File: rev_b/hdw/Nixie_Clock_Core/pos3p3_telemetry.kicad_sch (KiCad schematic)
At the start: 7 parts, among them U501 INA219BxDCN, U502 MCP9804

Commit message: lots of rev B control board schematic progress
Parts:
- renumbered C503 to C?, C502 to C?, C501 to C?, DOC501 to DOC?, DOC502 to DOC?, U502 to U?, U501 to U?

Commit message: more rev b sch progress
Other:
- moved on the sheet: C?

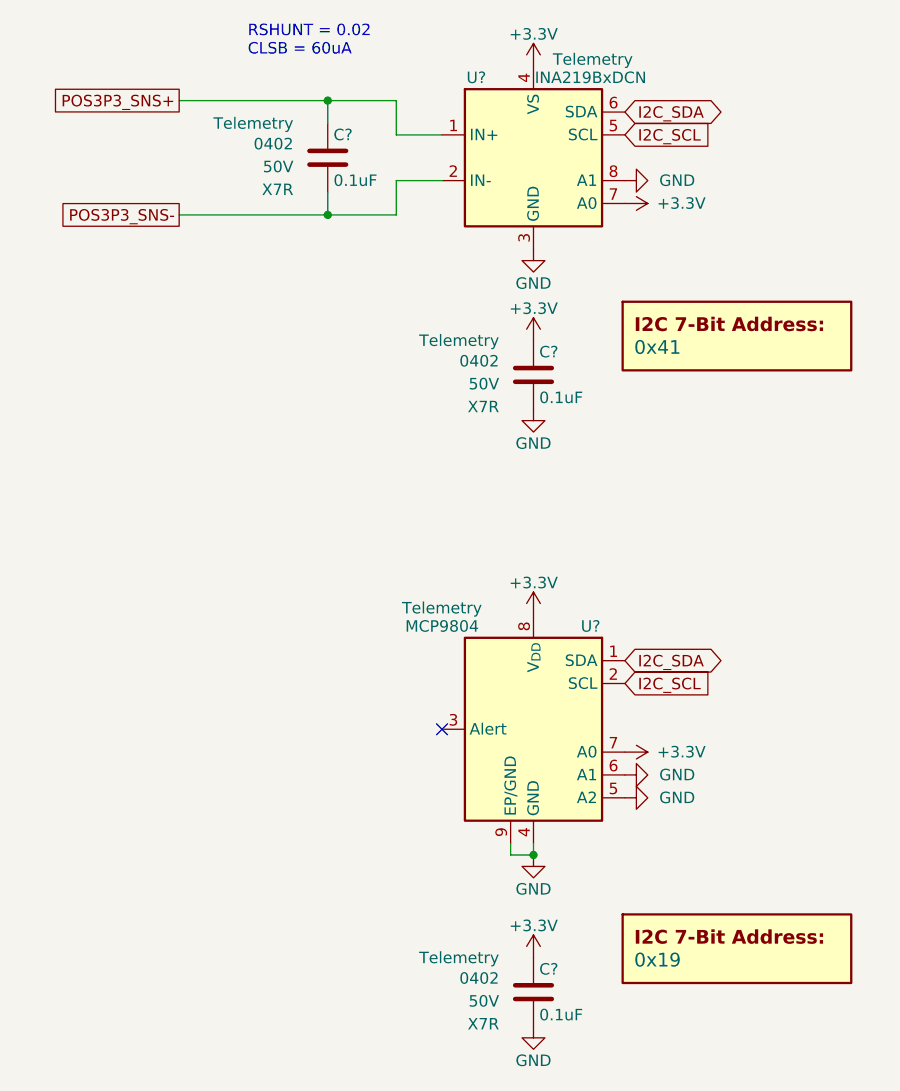
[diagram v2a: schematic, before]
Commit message: updated footprints, ran some DRC
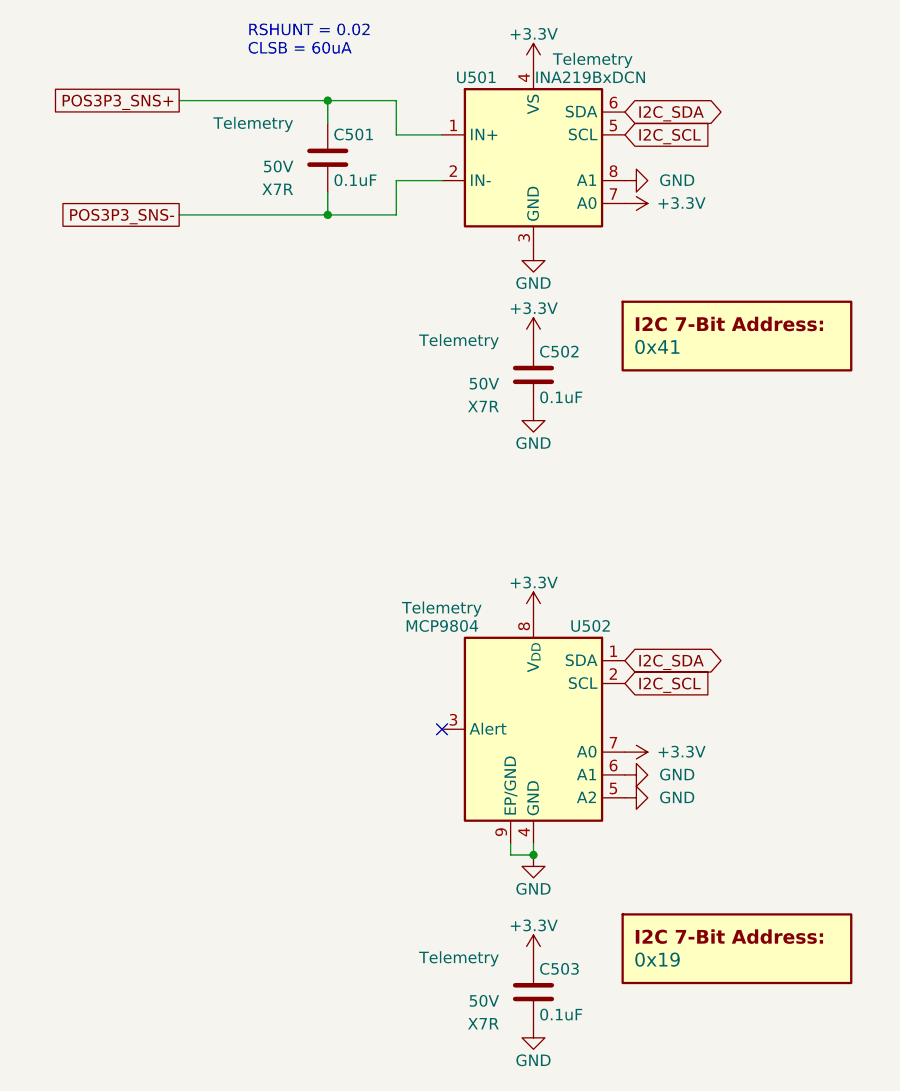
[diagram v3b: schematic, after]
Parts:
- C501, C502, C503: renamed from C?; footprint Capacitors_SMD:C_0402 -> Capacitors_SMD:C_0603; Digi-Key PN 490-10698-1-ND -> (none); display_footprint 0402 -> (none)
- gave numbers to parts that had none: 4

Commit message: hid all passive refdes on core PCB
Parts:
- C501, C502, C503: Digi-Key PN (none) -> 1276-1935-1-ND; display_footprint (none) -> 0603
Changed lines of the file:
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@@
       (effects (font (size 1.27 1.27)) hide)
     )
-    (property "display_footprint" "" (at 125.73 149.606 0)
+    (property "display_footprint" "0603" (at 125.73 149.606 0)
       (effects (font (size 1.27 1.27)) (justify right))
     )
@@
       (effects (font (size 1.27 1.27)) (justify right))
     )
-    (property "Digi-Key PN" "" (at 129.54 151.13 0)
+    (property "Digi-Key PN" "1276-1935-1-ND" (at 129.54 151.13 0)
       (effects (font (size 1.27 1.27)) hide)
     )
@@
       (effects (font (size 1.27 1.27)) hide)
     )
-    (property "display_footprint" "" (at 125.73 81.026 0)
+    (property "display_footprint" "0603" (at 125.73 81.026 0)
       (effects (font (size 1.27 1.27)) (justify right))
     )
@@
       (effects (font (size 1.27 1.27)) (justify right))
     )
-    (property "Digi-Key PN" "" (at 129.54 82.55 0)
+    (property "Digi-Key PN" "1276-1935-1-ND" (at 129.54 82.55 0)
       (effects (font (size 1.27 1.27)) hide)
     )
@@
       (effects (font (size 1.27 1.27)) hide)
     )
-    (property "display_footprint" "" (at 102.87 56.896 0)
+    (property "display_footprint" "0603" (at 102.87 56.896 0)
       (effects (font (size 1.27 1.27)) (justify right))
     )
@@
       (effects (font (size 1.27 1.27)) (justify right))
     )
-    (property "Digi-Key PN" "" (at 106.68 58.42 0)
-      (effects (font (size 1.27 1.27)) hide)
-    )
+    (property "Digi-Key PN" "1276-1935-1-ND" (at 106.68 58.42 0)
+      (effects (font (size 1.27 1.27)) hide)
+    )

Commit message: added BOM
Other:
- title: (none) -> Nixie Clock Redux Core Board
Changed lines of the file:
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@@
   (paper "A")
   (title_block
-    (date "2023-05-12")
-    (rev "PRELIM")
+    (title "Nixie Clock Redux Core Board")
+    (date "2023-07-30")
+    (rev "B")
     (company "Drew Maatman")
   )
@@
     (effects (font (size 1.27 1.27)) (justify left bottom))
   )
-  (global_label "POS3P3_SNS-" (shape passive) (at 90.17 64.77 180)
+  (global_label "POS3P3_SNS-" (shape passive) (at 90.17 64.77 180) (fields_autoplaced)
     (effects (font (size 1.27 1.27)) (justify right))
-    (property "Intersheetrefs" "${INTERSHEET_REFS}" (at 90.17 64.77 0)
-      (effects (font (size 1.27 1.27)) hide)
+    (property "Intersheetrefs" "${INTERSHEET_REFS}" (at 74.587 64.77 0)
+      (effects (font (size 1.27 1.27)) (justify right))
     )
   )
-  (global_label "I2C_SCL" (shape input) (at 139.7 55.88 0)
+  (global_label "I2C_SCL" (shape input) (at 139.7 55.88 0) (fields_autoplaced)
     (effects (font (size 1.27 1.27)) (justify left))
-    (property "Intersheetrefs" "${INTERSHEET_REFS}" (at 139.7 55.88 0)
-      (effects (font (size 1.27 1.27)) hide)
+    (property "Intersheetrefs" "${INTERSHEET_REFS}" (at 150.1653 55.88 0)
+      (effects (font (size 1.27 1.27)) (justify left))
     )
   )
-  (global_label "I2C_SCL" (shape input) (at 139.7 116.84 0)
+  (global_label "I2C_SCL" (shape input) (at 139.7 116.84 0) (fields_autoplaced)
     (effects (font (size 1.27 1.27)) (justify left))
-    (property "Intersheetrefs" "${INTERSHEET_REFS}" (at 139.7 116.84 0)
-      (effects (font (size 1.27 1.27)) hide)
+    (property "Intersheetrefs" "${INTERSHEET_REFS}" (at 150.1653 116.84 0)
+      (effects (font (size 1.27 1.27)) (justify left))
     )
   )
-  (global_label "I2C_SDA" (shape bidirectional) (at 139.7 53.34 0)
+  (global_label "I2C_SDA" (shape bidirectional) (at 139.7 53.34 0) (fields_autoplaced)
     (effects (font (size 1.27 1.27)) (justify left))
-    (property "Intersheetrefs" "${INTERSHEET_REFS}" (at 139.7 53.34 0)
-      (effects (font (size 1.27 1.27)) hide)
+    (property "Intersheetrefs" "${INTERSHEET_REFS}" (at 151.3371 53.34 0)
+      (effects (font (size 1.27 1.27)) (justify left))
     )
   )
-  (global_label "POS3P3_SNS+" (shape passive) (at 90.17 52.07 180)
+  (global_label "POS3P3_SNS+" (shape passive) (at 90.17 52.07 180) (fields_autoplaced)
     (effects (font (size 1.27 1.27)) (justify right))
-    (property "Intersheetrefs" "${INTERSHEET_REFS}" (at 90.17 52.07 0)
-      (effects (font (size 1.27 1.27)) hide)
+    (property "Intersheetrefs" "${INTERSHEET_REFS}" (at 74.587 52.07 0)
+      (effects (font (size 1.27 1.27)) (justify right))
     )
   )
-  (global_label "I2C_SDA" (shape bidirectional) (at 139.7 114.3 0)
+  (global_label "I2C_SDA" (shape bidirectional) (at 139.7 114.3 0) (fields_autoplaced)
     (effects (font (size 1.27 1.27)) (justify left))
-    (property "Intersheetrefs" "${INTERSHEET_REFS}" (at 139.7 114.3 0)
-      (effects (font (size 1.27 1.27)) hide)
+    (property "Intersheetrefs" "${INTERSHEET_REFS}" (at 151.3371 114.3 0)
+      (effects (font (size 1.27 1.27)) (justify left))
     )
   )
